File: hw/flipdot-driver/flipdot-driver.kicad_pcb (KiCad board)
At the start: 2 copper layers, 87 parts, among them J1 DISPLAY, J10 AUX_Power, J11 GND, J12 +VIN, J2 NRF_CON, J3 Prog, J4 I2C, J5 USART, J6 USB, J8 RST, J9 MAIN_Power, Q1 MMBTA64, Q10 MMBTA64, Q11 MMBTA64, Q12 MMBTA64, Q13 MMBTA64, Q14 MMBTA64, Q15 Q_NMOS_GSD, Q16 Q_NMOS_GSD, Q17 Q_NMOS_GSD, Q18 Q_NMOS_GSD, Q2 MMBTA64, Q3 MMBTA64, Q4 MMBTA64, Q5 MMBTA64, Q6 MMBTA64, Q7 MMBTA64, Q8 MMBTA64, Q9 MMBTA64, U1 AT25xxx, U2 ULN2003A, U3 USBLC6-2SC6, U4 AZ1117-3.3, U5 ULN2003A, U6 stm32_STM32F103C(8-B)Tx, Y1 32768, Y2 8MHz/20pF

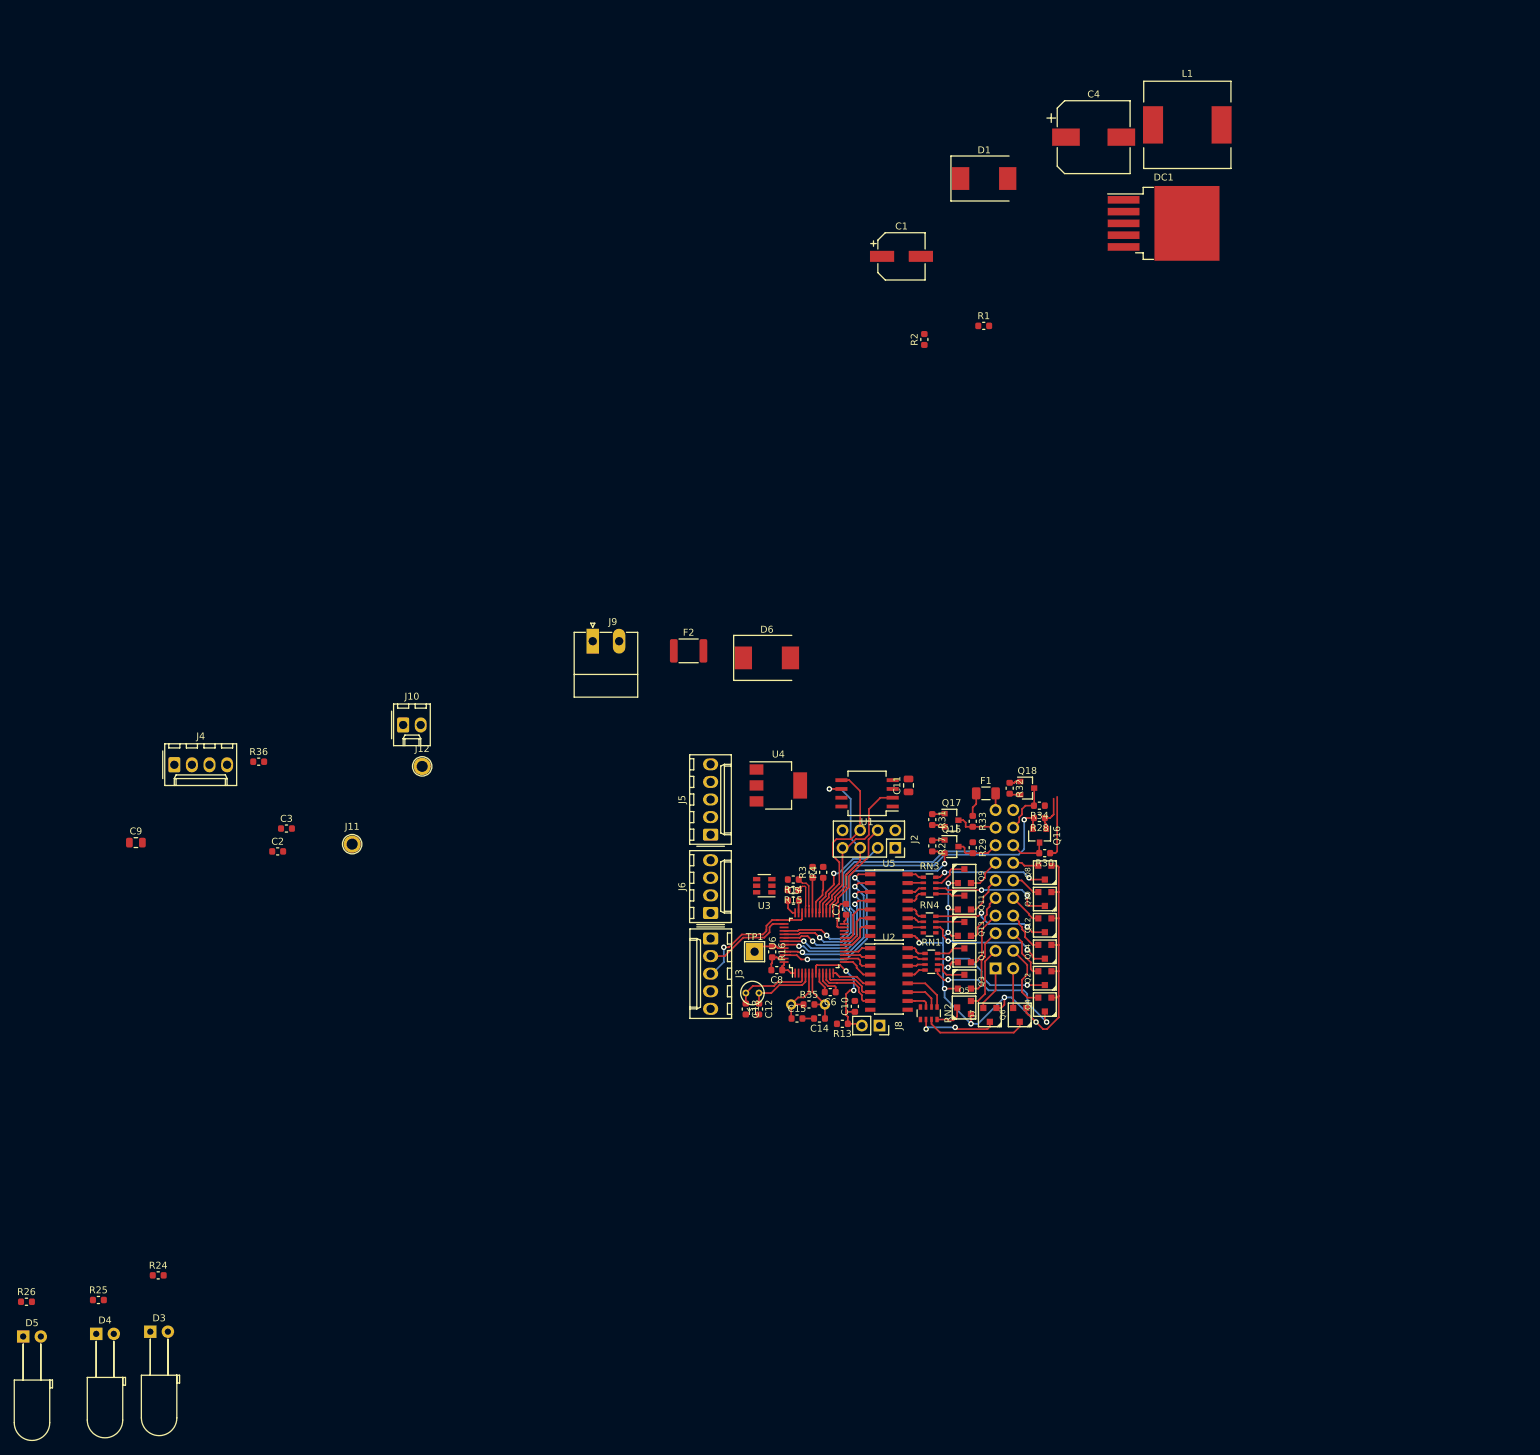
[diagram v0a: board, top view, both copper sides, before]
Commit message: Added 74HC595 and AX5201
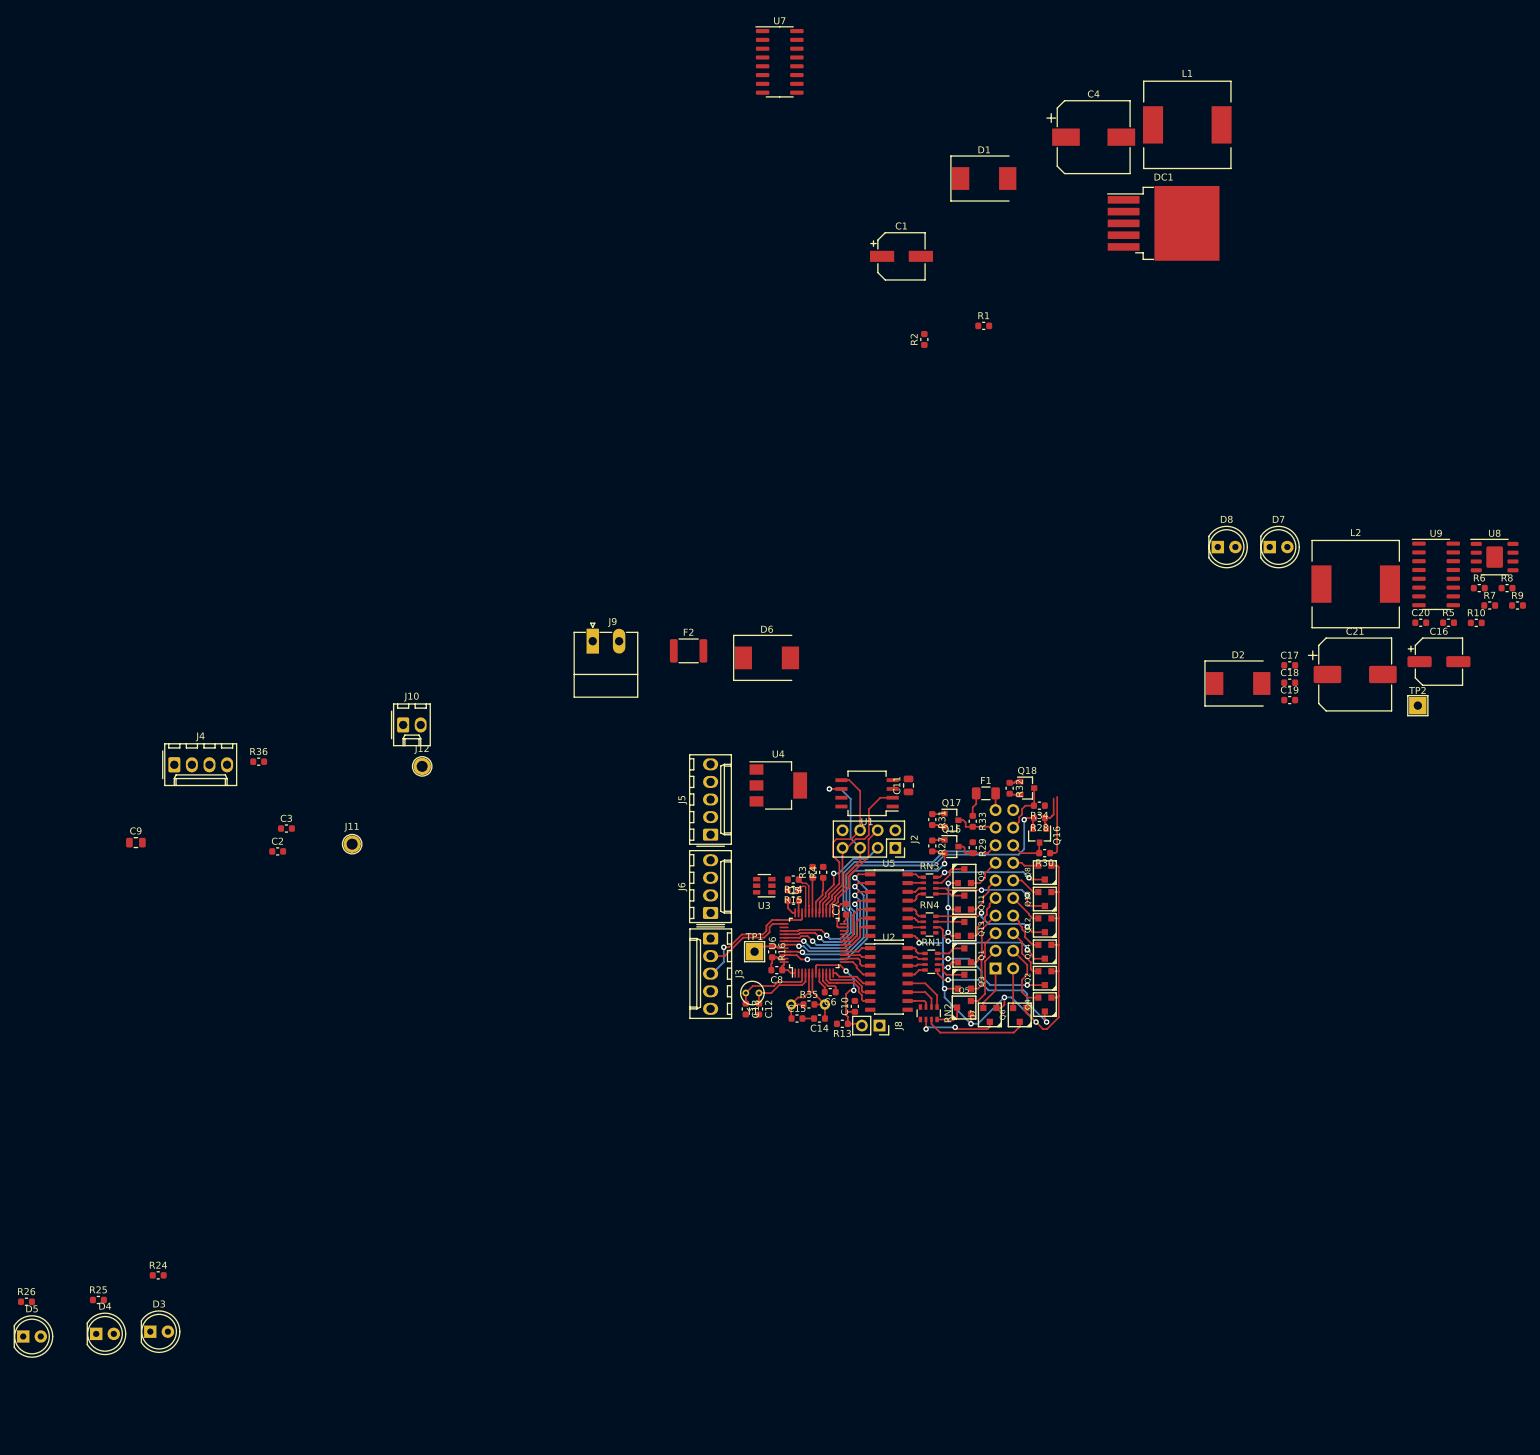
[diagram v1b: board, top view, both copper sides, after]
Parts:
- added C16: 470u, Capacitor_SMD:CP_Elec_6.3x5.3, F.Cu at (258.8, 12.5)
- added C17: 100n, Capacitor_SMD:C_0603_1608Metric, F.Cu at (237.3, 13.0)
- added C18: 470n, Capacitor_SMD:C_0603_1608Metric, F.Cu at (237.3, 15.5)
- added C19: 470n, Capacitor_SMD:C_0603_1608Metric, F.Cu at (237.3, 18.0)
- added C20: 1u, Capacitor_SMD:C_0603_1608Metric, F.Cu at (256.2, 6.86)
- added C21: 220u, Capacitor_SMD:CP_Elec_10x10, F.Cu at (246.7, 14.3)
- added D2: SK34, Diode_SMD:D_SMC, F.Cu at (229.9, 15.6)
- added D7: LED, LED_THT:LED_D5.0mm, F.Cu at (234.4, -4.07)
- added D8: LED, LED_THT:LED_D5.0mm, F.Cu at (226.9, -4.07)
- added L2: 68u, Inductor_SMD:L_12x12mm_H8mm, F.Cu at (246.8, 1.28)
- added R10: 12k, Resistor_SMD:R_0603_1608Metric, F.Cu at (264.2, 6.88)
- added R5: 12k, Resistor_SMD:R_0603_1608Metric, F.Cu at (260.2, 6.86)
- added R6: 30k, Resistor_SMD:R_0603_1608Metric, F.Cu at (264.7, 1.86)
- added R7: 1.3k, Resistor_SMD:R_0603_1608Metric, F.Cu at (266.2, 4.37)
- added R8: 330R, Resistor_SMD:R_0603_1608Metric, F.Cu at (268.7, 1.86)
- added R9: 330R, Resistor_SMD:R_0603_1608Metric, F.Cu at (270.2, 4.37)
- added TP2: TestPoint, TestPoint:TestPoint_THTPad_2.5x2.5mm_Drill1.2mm, F.Cu at (255.8, 18.8)
- added U7: 74HC595, Package_SO:SOIC-16_3.9x9.9mm_P1.27mm, F.Cu at (163.7, -74.1)
- added U8: AX5201, Package_SO:HSOP-8-1EP_3.9x4.9mm_P1.27mm_EP2.41x3.1mm, F.Cu at (266.9, -2.62)
- added U9: 74HC595, Package_SO:SOIC-16_3.9x9.9mm_P1.27mm, F.Cu at (258.4, -0.12)
- D3, D4, D5: footprint LED_THT:LED_D5.0mm_Horizontal_O6.35mm_Z9.0mm -> LED_THT:LED_D5.0mm
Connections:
- net Net-(R14-Pad2) renamed /USB1_N
- J2 pad 8: /NRF_IRQ -> (no net)
- J5 pad 2: Net-(J5-Pad2) -> (no net)
- RN2 pad 4: Net-(RN2-Pad4) -> (no net)
- RN2 pad 5: Net-(RN2-Pad5) -> (no net)
- RN4 pad 4: Net-(RN4-Pad4) -> (no net)
- RN4 pad 5: Net-(RN4-Pad5) -> (no net)
- U2 pad 1: /LV_R1N -> Net-(U2-Pad1)
- U2 pad 2: /LV_R2N -> Net-(U2-Pad2)
- U2 pad 3: /LV_R3N -> Net-(U2-Pad3)
- U2 pad 4: /LV_R4N -> Net-(U2-Pad4)
- U2 pad 5: /LV_R5N -> Net-(U2-Pad5)
- U2 pad 6: /LV_R6N -> Net-(U2-Pad6)
- U2 pad 7: /LV_R7N -> Net-(U2-Pad7)
- U5 pad 1: /LV_R1P -> Net-(U5-Pad1)
- U5 pad 2: /LV_R2P -> Net-(U5-Pad2)
- U5 pad 3: /LV_R3P -> Net-(U5-Pad3)
- U5 pad 4: /LV_R4P -> Net-(U5-Pad4)
- U5 pad 5: /LV_R5P -> Net-(U5-Pad5)
- U5 pad 6: /LV_R6P -> Net-(U5-Pad6)
- U5 pad 7: /LV_R7P -> Net-(U5-Pad7)
- U6 pad 10: /LV_R7N -> (no net)
- U6 pad 11: /LV_R6N -> /LED1
- U6 pad 12: /LV_R5N -> /LED2
- U6 pad 13: /LV_R4N -> (no net)
- U6 pad 14: /LV_R3N -> (no net)
- U6 pad 15: /LV_R2N -> (no net)
- U6 pad 16: /LV_R1N -> /24V_EN
- U6 pad 18: /LV_R7P -> (no net)
- U6 pad 19: /LV_R6P -> (no net)
- U6 pad 2: /LV_RST -> (no net)
- U6 pad 20: /LV_R5P -> /BOOT1
- U6 pad 38: /24V_EN -> /~SR_OE
- U6 pad 39: /LV_CLK -> /SR_CLK
- U6 pad 40: /LV_RET -> /SR_STROBE
- U6 pad 41: /LV_DATA -> /SR_DATA1
- U6 pad 42: /LV_R4P -> (no net)
- U6 pad 43: /LV_R3P -> /LV_CLK
- U6 pad 45: /LV_R2P -> /LV_DATA
- U6 pad 46: /LV_R1P -> /LV_RET
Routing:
- net /LV_CLK: track 41.0 -> 1.60 mm, vias 1 -> 0
- net /SR_CLK: track 0.00 -> 39.4 mm, vias 0 -> 1
- net Net-(U5-Pad4): track 0.00 -> 18.8 mm, vias 0 -> 2
- net /LV_R4P: track 18.8 -> 0.00 mm, vias 2 -> 0
- net Net-(U2-Pad7): track 0.00 -> 9.34 mm
- net /LV_R7N: track 9.34 -> 0.00 mm
- net Net-(U2-Pad6): track 0.00 -> 7.86 mm
- net /LV_R6N: track 7.86 -> 0.00 mm
- net Net-(U5-Pad6): track 0.00 -> 6.33 mm
- net /LV_R6P: track 6.33 -> 0.00 mm
- net Net-(U2-Pad5): track 0.00 -> 5.96 mm
- net /LV_R5N: track 5.96 -> 0.00 mm
- net Net-(U5-Pad7): track 0.00 -> 5.49 mm
- net /LV_R7P: track 5.49 -> 0.00 mm
- net Net-(U2-Pad4): track 0.00 -> 4.67 mm
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
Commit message: Routed, with unused parts.
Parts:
- removed R14, R15: 22R, Resistor_SMD:R_0603_1608Metric
- added C22: 100n, Capacitor_SMD:C_0603_1608Metric, F.Cu at (143.1, 67.3)
- added C23: 680u, Capacitor_THT:CP_Radial_D10.0mm_P5.00mm, B.Cu at (185.7, 60.2)
- added J7: USB_B_Micro, stm32_converter_footprints:USB_Micro-B, F.Cu at (162.7, 69.9)
- added R11: 1k5, Resistor_SMD:R_0603_1608Metric, F.Cu at (144.1, 47.9)
- added R12: 1k5, Resistor_SMD:R_0603_1608Metric, F.Cu at (139.9, 47.0)
- added RN5: 22R, Resistor_SMD:R_Array_Convex_2x0402, F.Cu at (162.3, 62.1)
- C16: value 470u -> 680u; footprint Capacitor_SMD:CP_Elec_6.3x5.3 -> Capacitor_THT:CP_Radial_D10.0mm_P5.00mm; moved to B.Cu
- C21: value 220u -> 680u; footprint Capacitor_SMD:CP_Elec_10x10 -> Capacitor_THT:CP_Radial_D10.0mm_P5.00mm; moved to B.Cu
- D3, D4, D5: footprint LED_THT:LED_D5.0mm -> LED_THT:LED_D3.0mm
- D7, D8: footprint LED_THT:LED_D5.0mm -> LED_THT:LED_D3.0mm; moved to B.Cu
- J2, J3, J4, J5, J6, J8, J9: moved to B.Cu
- moved D3 253.4 mm to (203.5, -107.9)
- moved D4 253.4 mm to (195.7, -107.6)
- moved R24 253.4 mm to (204.6, -116.0)
- moved R25 253.4 mm to (196.0, -112.5)
- moved D5 253.4 mm to (185.1, -107.2)
- moved R26 253.4 mm to (185.6, -112.2)
- moved C2 190.1 mm to (192.2, -121.1)
- moved C3 190.1 mm to (193.4, -124.4)
- moved J10 190.1 mm to (210.3, -139.4)
- moved J11 190.1 mm to (202.9, -122.2)
- moved J12 190.1 mm to (213.0, -133.4)
- moved R8 132.8 mm to (146.3, 53.6), turned to 90 degrees
- moved U7 131.4 mm to (171.8, 57.0), turned to 180 degrees
- moved R9 128.7 mm to (151.1, 53.3), turned to 90 degrees
- moved R5 113.1 mm to (156.0, 50.7), turned to 180 degrees
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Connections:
- net Net-(J6-Pad2) renamed /USB2_P
- net Net-(J6-Pad3) renamed /USB2_N
- J2 pad 8: (no net) -> /NRF_IRQ
- J5 pad 2: (no net) -> Net-(J5-Pad2)
- RN2 pad 4: (no net) -> Net-(RN2-Pad4)
- RN2 pad 5: (no net) -> Net-(RN2-Pad5)
- RN4 pad 4: (no net) -> Net-(RN4-Pad4)
- RN4 pad 5: (no net) -> Net-(RN4-Pad5)
- U6 pad 10: (no net) -> Net-(U6-Pad10)
- U6 pad 13: (no net) -> Net-(U6-Pad13)
- U6 pad 14: (no net) -> Net-(U6-Pad14)
- U6 pad 15: (no net) -> Net-(U6-Pad15)
- U6 pad 18: (no net) -> Net-(U6-Pad18)
- U6 pad 19: (no net) -> Net-(U6-Pad19)
- U6 pad 2: (no net) -> Net-(U6-Pad2)
- U6 pad 42: (no net) -> /LV_RST
- U7 pad 15: (no net) -> Net-(U7-Pad15)
- U9 pad 15: (no net) -> Net-(U9-Pad15)
- U9 pad 9: (no net) -> Net-(U9-Pad9)
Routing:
- net +3V3: track 22.0 -> 355.6 mm, vias 0 -> 10
- net +12V: track 12.5 -> 147.7 mm, vias 0 -> 6
- net /LV_CLK: track 1.60 -> 66.0 mm, vias 0 -> 2
- net /LV_RST: track 1.88 -> 61.1 mm, vias 0 -> 2
- net GND: track 15.5 -> 71.6 mm, vias 0 -> 9
- net +24V: track 88.6 -> 143.5 mm, vias 9 -> 10
- net /24V_EN: track 0.00 -> 42.5 mm, vias 0 -> 2
- net /BOOT1: track 0.00 -> 39.3 mm, vias 0 -> 1
- net /NRST: track 18.2 -> 55.4 mm, vias 2 -> 1
- net Net-(J6-Pad4): track 0.00 -> 33.5 mm
- net /I2C_SDA: track 0.00 -> 29.4 mm
- net Net-(R16-Pad1): track 4.70 -> 33.5 mm, vias 0 -> 2
- net /SWDIO: track 19.0 -> 44.9 mm, vias 1 -> 3
- net /LV_R1P: track 25.4 -> 0.00 mm, vias 2 -> 0
- net Net-(D2-Pad2): track 0.00 -> 24.0 mm
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- added copper zone on B.Cu, net GND
- added copper zone on F.Cu, net GND
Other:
- board outline added: 67.5 x 49.5 mm

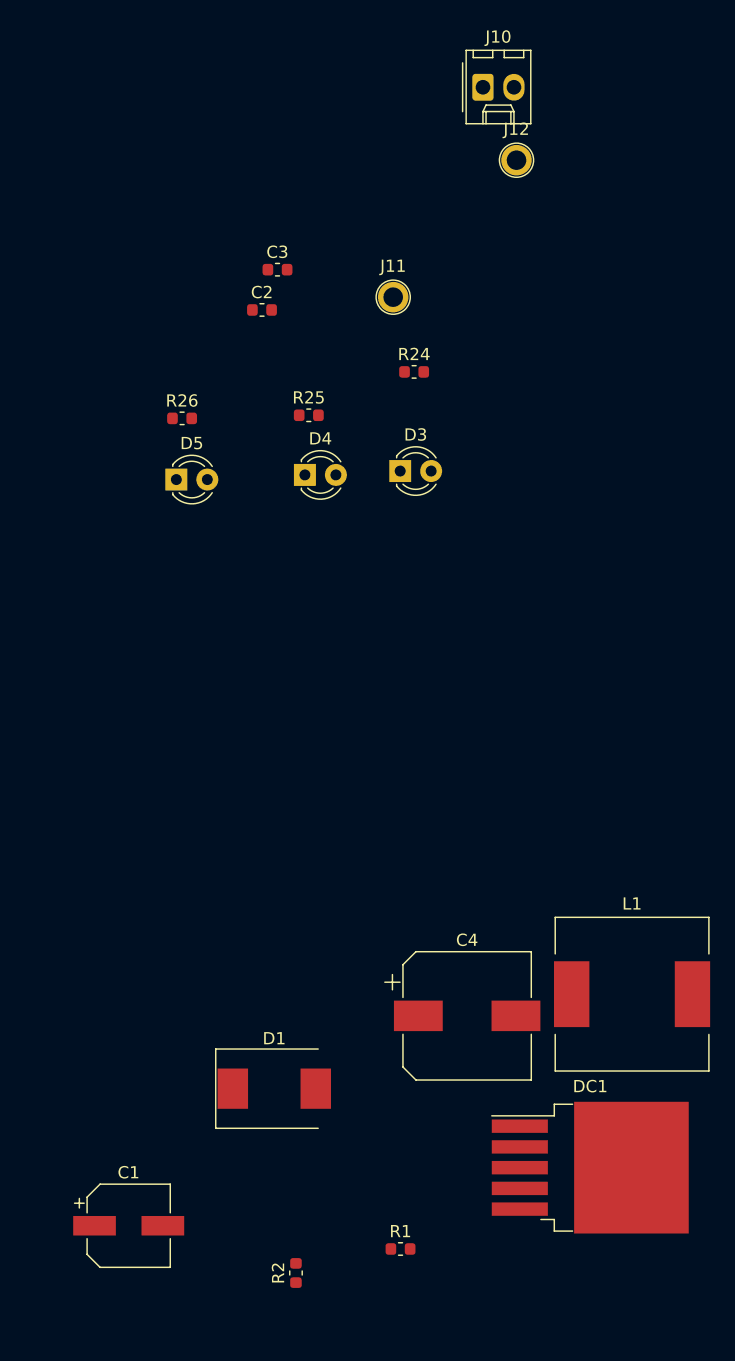
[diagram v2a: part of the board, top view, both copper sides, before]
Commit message: Routed, without unused parts.
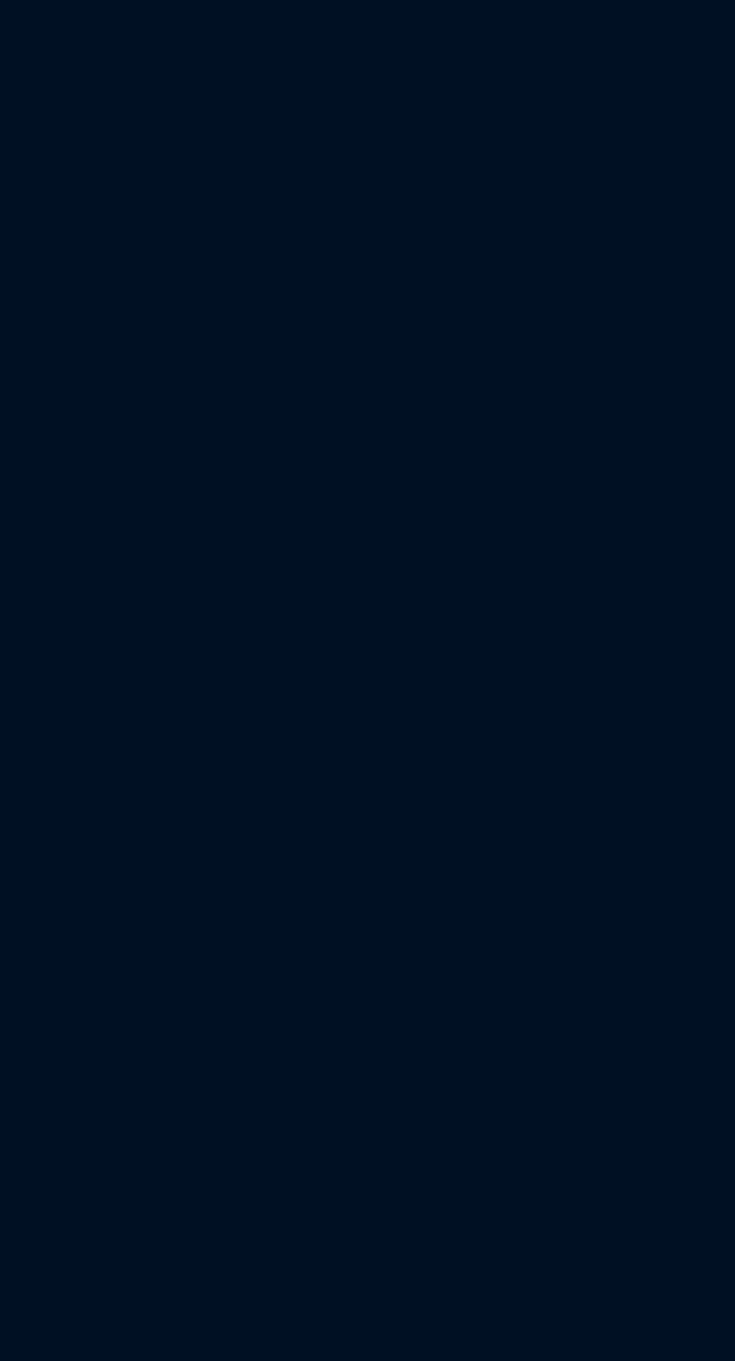
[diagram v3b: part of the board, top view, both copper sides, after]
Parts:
- removed C1: 100u, Capacitor_SMD:CP_Elec_6.3x5.3
- removed C2, C3: 1u, Capacitor_SMD:C_0603_1608Metric
- removed C4: 220u, Capacitor_SMD:CP_Elec_10x10
- removed D1: SK33, Diode_SMD:D_SMC
- removed D3, D4, D5: LED, LED_THT:LED_D3.0mm
- removed DC1: XL6009, Package_TO_SOT_SMD:TO-263-5_TabPin3
- removed J10: AUX_Power, Connector_Molex:Molex_KK-254_AE-6410-02A_1x02_P2.54mm_Vertical
- removed J11: GND, user:TestPoint_Plated_Hole_D1.6mm
- removed J12: +VIN, user:TestPoint_Plated_Hole_D1.6mm
- removed L1: 33u, Inductor_SMD:L_12x12mm_H8mm
- removed R1: 12k, Resistor_SMD:R_0603_1608Metric
- removed R2: 680R, Resistor_SMD:R_0603_1608Metric
- removed R24: 1k5, Resistor_SMD:R_0603_1608Metric
- removed R25: 330R, Resistor_SMD:R_0603_1608Metric
- removed R26: 4k7, Resistor_SMD:R_0603_1608Metric
